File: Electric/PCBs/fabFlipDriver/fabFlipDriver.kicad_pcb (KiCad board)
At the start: 2 copper layers, 45 x 70 mm, 91 parts, among them J1 Conn_02x05_Odd_Even, J2 Conn_02x05_Odd_Even, J3 Conn_01x08, J4 Conn_01x08, J5 Conn_01x02, J6 Conn_01x02, J7 Conn_01x02, Q1 AO3401A, Q10 AO3401A, Q11 2N7002, Q12 2N7002, Q13 AO3401A, Q14 AO3401A, Q15 2N7002, Q16 2N7002, Q17 AO3401A, Q18 AO3401A, Q19 2N7002, Q2 AO3401A, Q20 2N7002, Q21 AO3401A, Q22 AO3401A, Q23 2N7002, Q24 2N7002, Q25 AO3401A, Q26 AO3401A, Q27 2N7002, Q28 2N7002, Q29 AO3401A, Q3 2N7002, Q30 AO3401A, Q31 2N7002, Q32 2N7002, Q4 2N7002, Q5 AO3401A, Q6 AO3401A, Q7 2N7002, Q8 2N7002, Q9 AO3401A, U1 74HC595, U2 74HC595

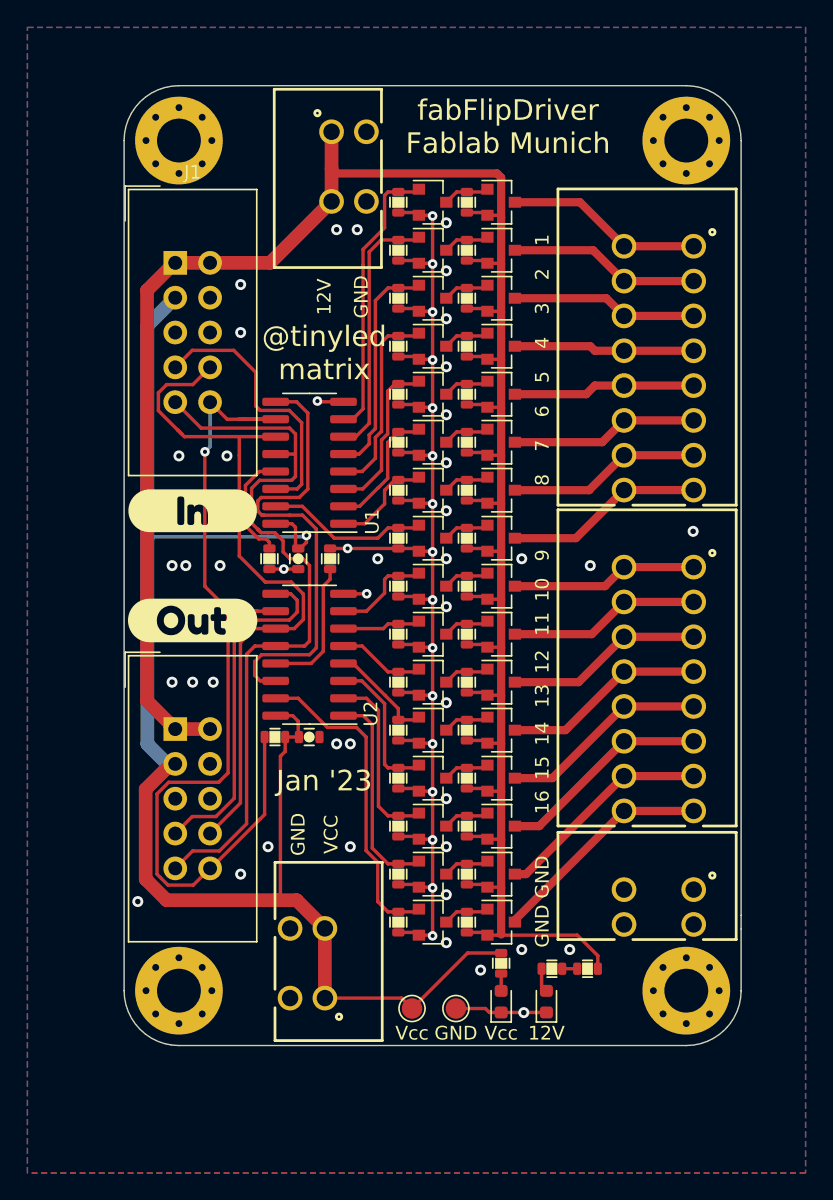
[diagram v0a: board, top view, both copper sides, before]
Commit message: PCB design finalized
DRC okay
should be ready for production
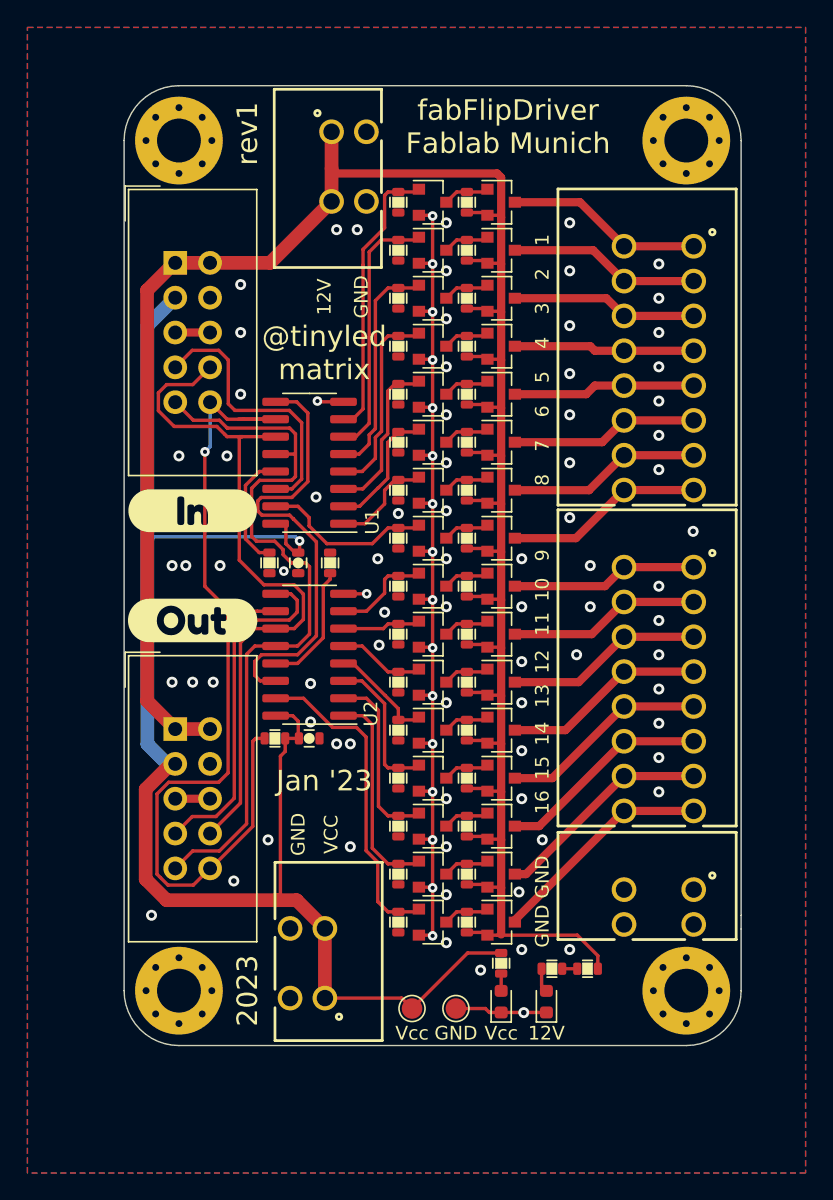
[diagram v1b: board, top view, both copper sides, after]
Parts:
- moved C1 0.30 mm to (116.2, 149.3)
- moved R23 0.30 mm to (118.5, 149.3)
- moved R9 0.30 mm to (114.1, 149.3)
- moved C2 0.10 mm to (117.0, 162.1)
- moved R18 0.10 mm to (114.5, 162.1)
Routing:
- net GND: track 111.6 -> 84.3 mm, vias 60 -> 96
- net VCC: track 113.7 -> 110.6 mm
- net Net-(U1-Pad9): track 34.2 -> 32.7 mm
- net /Clear: track 67.3 -> 68.2 mm
- net Net-(R23-Pad1): track 10.0 -> 9.17 mm
- net /Logic08: track 11.8 -> 12.5 mm
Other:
- board text added: "2023"
- board text added: "rev1"

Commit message: PCB update
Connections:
- net /Logic01 renamed /Bit08
- net /Logic02 renamed /Bit09
- net /Logic03 renamed /Bit10
- net /Logic04 renamed /Bit11
- net /Logic05 renamed /Bit12
- net /Logic06 renamed /Bit13
- net /Logic07 renamed /Bit14
- net /Logic08 renamed /Bit15
- net /Logic09 renamed /Bit00
- net /Logic10 renamed /Bit01
- net /Logic11 renamed /Bit02
- net /Logic12 renamed /Bit03
- net /Logic13 renamed /Bit04
- net /Logic14 renamed /Bit05
- net /Logic15 renamed /Bit06
- net /Logic16 renamed /Bit07
- net /Out01 renamed /O_08
- net /Out02 renamed /O_09
- net /Out03 renamed /O_10
- net /Out04 renamed /O_11
- net /Out05 renamed /O_12
- net /Out06 renamed /O_13
- net /Out07 renamed /O_14
- net /Out08 renamed /O_15
- net /Out09 renamed /O_00
- net /Out10 renamed /O_01
- net /Out11 renamed /O_02
- net /Out12 renamed /O_03
- net /Out13 renamed /O_04
- net /Out14 renamed /O_05
- net /Out15 renamed /O_06
- net /Out16 renamed /O_07
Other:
- board text added: "0"
- board text removed: "16"

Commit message: Small changes
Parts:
- added D10: D, Diode_SMD:D_SOD-523, F.Cu at (131.7, 159.8)
- added D11: D, Diode_SMD:D_SOD-523, F.Cu at (131.7, 135.2)
- added D12: D, Diode_SMD:D_SOD-523, F.Cu at (131.7, 163.2)
- added D13: D, Diode_SMD:D_SOD-523, F.Cu at (131.7, 138.8)
- added D14: D, Diode_SMD:D_SOD-523, F.Cu at (131.7, 166.8)
- added D15: D, Diode_SMD:D_SOD-523, F.Cu at (131.7, 142.2)
- added D16: D, Diode_SMD:D_SOD-523, F.Cu at (131.7, 170.2)
- added D17: D, Diode_SMD:D_SOD-523, F.Cu at (131.7, 145.8)
- added D18: D, Diode_SMD:D_SOD-523, F.Cu at (131.7, 173.8)
- added D3: D, Diode_SMD:D_SOD-523, F.Cu at (131.7, 121.2)
- added D4: D, Diode_SMD:D_SOD-523, F.Cu at (131.7, 149.2)
- added D5: D, Diode_SMD:D_SOD-523, F.Cu at (131.7, 124.8)
- added D6: D, Diode_SMD:D_SOD-523, F.Cu at (131.7, 152.8)
- added D7: D, Diode_SMD:D_SOD-523, F.Cu at (131.7, 128.2)
- added D8: D, Diode_SMD:D_SOD-523, F.Cu at (131.7, 156.2)
- added D9: D, Diode_SMD:D_SOD-523, F.Cu at (131.7, 131.8)
- moved R1 3.71 mm to (127.1, 123.9), turned to 180 degrees
- moved R10 3.71 mm to (127.1, 130.9), turned to 180 degrees
- moved R12 3.71 mm to (127.1, 158.9), turned to 180 degrees
- moved R14 3.71 mm to (127.1, 134.4), turned to 180 degrees
- moved R16 3.71 mm to (127.1, 162.4), turned to 180 degrees
- moved R19 3.71 mm to (127.1, 137.9), turned to 180 degrees
- moved R21 3.71 mm to (127.1, 165.9), turned to 180 degrees
- moved R24 3.71 mm to (127.1, 141.4), turned to 180 degrees
- moved R26 3.71 mm to (127.1, 169.4), turned to 180 degrees
- moved R28 3.71 mm to (127.1, 144.9), turned to 180 degrees
- moved R3 3.71 mm to (127.1, 151.9), turned to 180 degrees
- moved R30 3.71 mm to (127.1, 172.9), turned to 180 degrees
- moved R32 3.71 mm to (127.1, 148.4), turned to 180 degrees
- moved R34 3.71 mm to (127.1, 176.4), turned to 180 degrees
- moved R5 3.71 mm to (127.1, 127.4), turned to 180 degrees
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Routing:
- net GND: track 84.3 -> 15.4 mm, vias 96 -> 106
- net +12V: track 175.1 -> 229.3 mm
- net /Bit08: track 20.6 -> 25.8 mm
- net /Bit13: track 8.36 -> 11.9 mm
- net /Bit09: track 18.8 -> 22.2 mm
- net /Bit05: track 12.2 -> 15.4 mm
- net /Bit12: track 10.9 -> 14.0 mm
- net /Bit14: track 6.49 -> 9.39 mm
- net /Bit10: track 16.5 -> 19.1 mm
- net /Bit00: track 6.24 -> 8.92 mm
- net /Bit11: track 13.4 -> 16.0 mm
- net /Bit04: track 9.81 -> 12.3 mm
- net /Bit03: track 7.77 -> 10.2 mm
- net /Bit07: track 23.5 -> 25.9 mm
- net /Bit15: track 12.5 -> 14.9 mm
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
